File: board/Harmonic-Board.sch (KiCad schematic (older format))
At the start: 10 parts

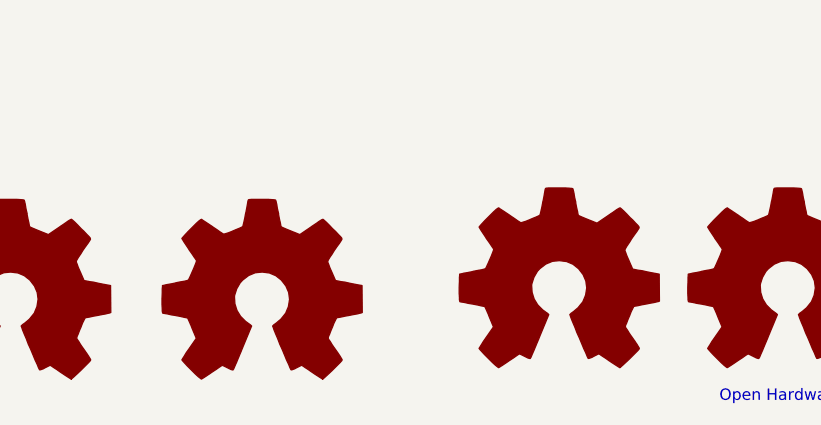
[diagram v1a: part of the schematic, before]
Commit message: - Added connector lib - added footprint for schottkey diode - added keep-out for new display
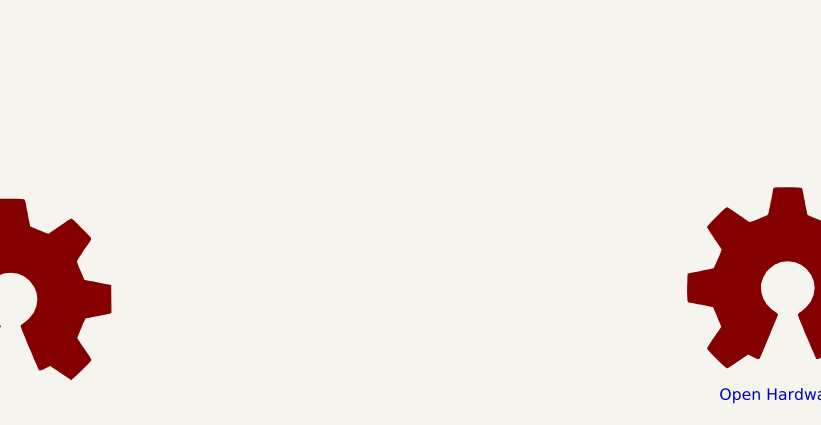
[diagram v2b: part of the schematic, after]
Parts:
- removed LOGO2: Logo_Open_Hardware_Large, badge:artwork-top-2, symbol Graphic:Logo_Open_Hardware_Large
- removed LOGO3: Logo_Open_Hardware_Large, badge:artwork-top, symbol Graphic:Logo_Open_Hardware_Large
- FID2: footprint Mechanical:Fiducial -> Fiducial:Fiducial_1mm_Mask2mm
- LOGO4: footprint badge:artwork-top-3 -> badge:artwork-top
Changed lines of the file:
@@
 F 0 "FID2" H 1150 7100 50  0000 C CNN
 F 1 "Fiducial" H 1150 7025 50  0000 C CNN
-F 2 "Mechanical:Fiducial" H 1150 6900 50  0001 C CNN
+F 2 "Fiducial:Fiducial_1mm_Mask2mm" H 1150 6900 50  0001 C CNN
 F 3 "~" H 1150 6900 50  0001 C CNN
 	1    1150 6900
@@
 F 0 "LOGO4" H 2750 7500 50  0001 C CNN
 F 1 "Logo_Open_Hardware_Large" H 2750 6600 50  0001 C CNN
-F 2 "badge:artwork-top-3" H 2750 7000 50  0001 C CNN
+F 2 "badge:artwork-top" H 2750 7000 50  0001 C CNN
 F 3 "~" H 2750 7000 50  0001 C CNN
 	1    2750 7000
 	1    0    0    -1
 $EndComp
-$Comp
-L Graphic:Logo_Open_Hardware_Large LOGO3
-U 1 1 5D1FAE2B
-P 3850 7000
-F 0 "LOGO3" H 3850 7500 50  0001 C CNN
-F 1 "Logo_Open_Hardware_Large" H 3850 6600 50  0001 C CNN
-F 2 "badge:artwork-top" H 3850 7000 50  0001 C CNN
-F 3 "~" H 3850 7000 50  0001 C CNN
-	1    3850 7000
-	1    0    0    -1
-$EndComp
-$Comp
-L Graphic:Logo_Open_Hardware_Large LOGO2
-U 1 1 5D1B414E
-P 5150 6950
-F 0 "LOGO2" H 5150 7450 50  0001 C CNN
-F 1 "Logo_Open_Hardware_Large" H 5150 6550 50  0001 C CNN
-F 2 "badge:artwork-top-2" H 5150 6950 50  0001 C CNN
-F 3 "~" H 5150 6950 50  0001 C CNN
-	1    5150 6950
-	1    0    0    -1
-$EndComp
